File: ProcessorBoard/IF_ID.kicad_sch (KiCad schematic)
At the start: 7 parts, among them U60 74ABT32, U61 74ABT16374, U62 74ABT16374

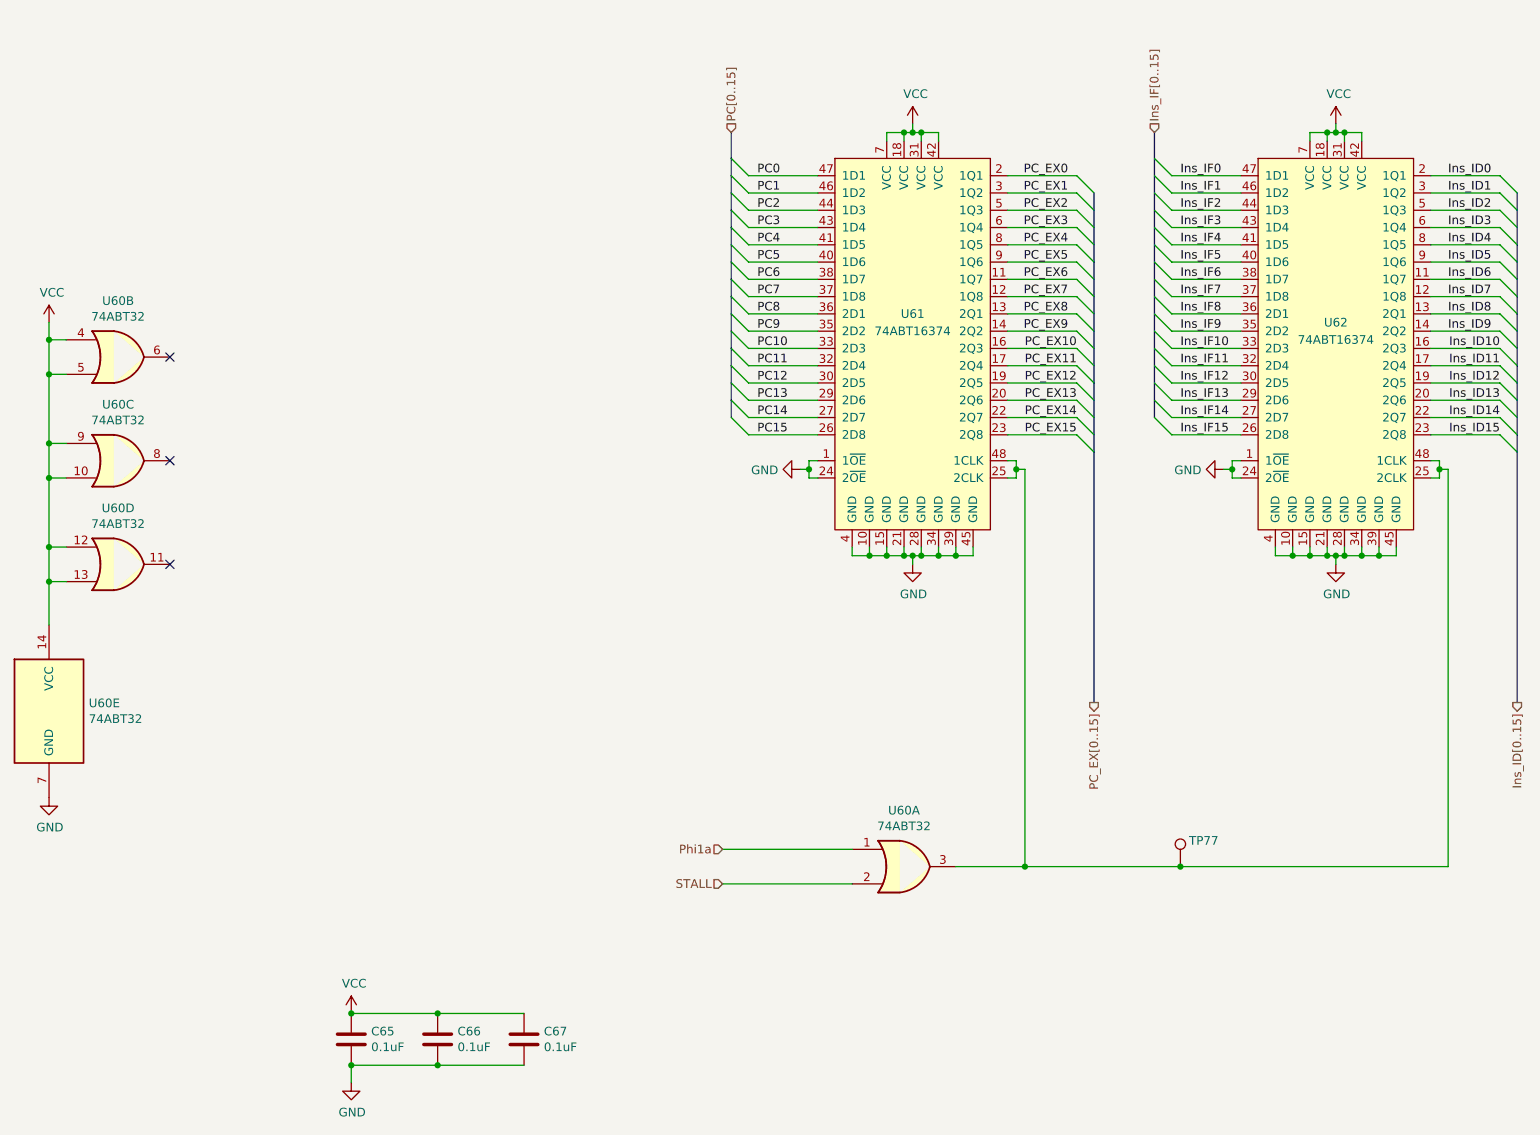
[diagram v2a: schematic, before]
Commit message: ProcessorBoard: update to include M/S bug fix in register file
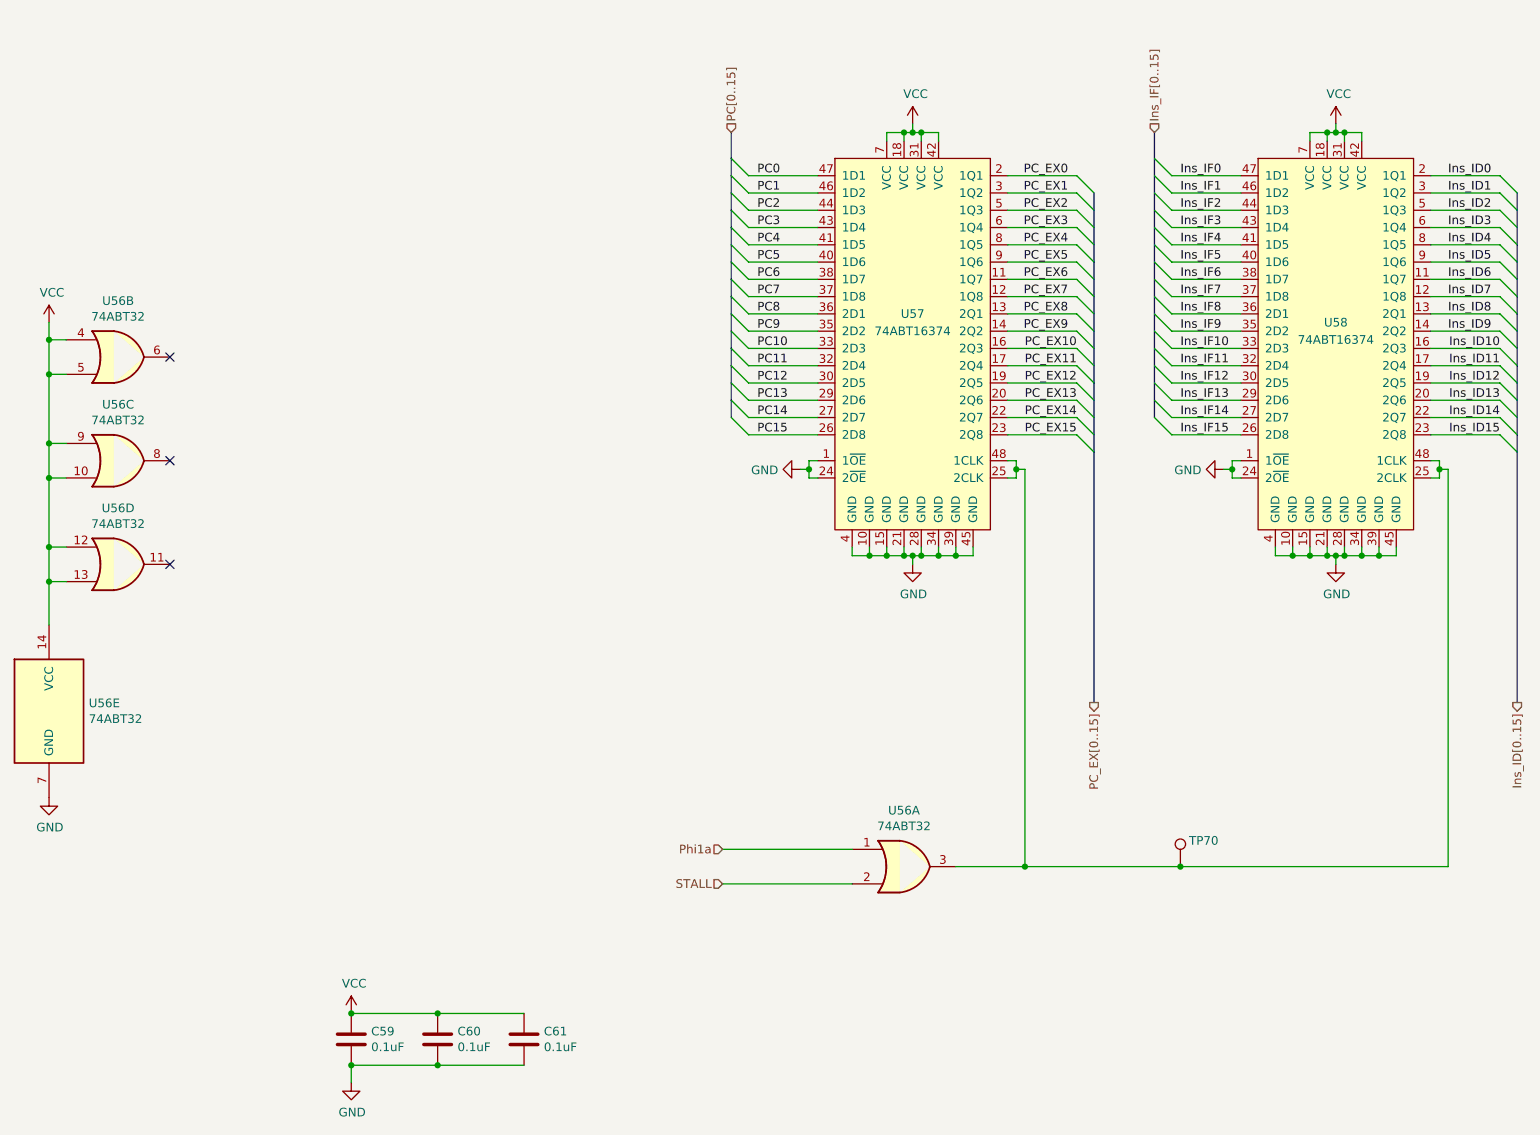
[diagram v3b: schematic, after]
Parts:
- renumbered C65 to C59, C66 to C60, C67 to C61, TP77 to TP70, U60 to U56, U61 to U57, U62 to U58

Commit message: ProcessorBoard: Replace Instruction ROM with a header for a daughter board
ROMs will be relocated to a daughter board to allow the memories and their
sockets to be swapped easily.
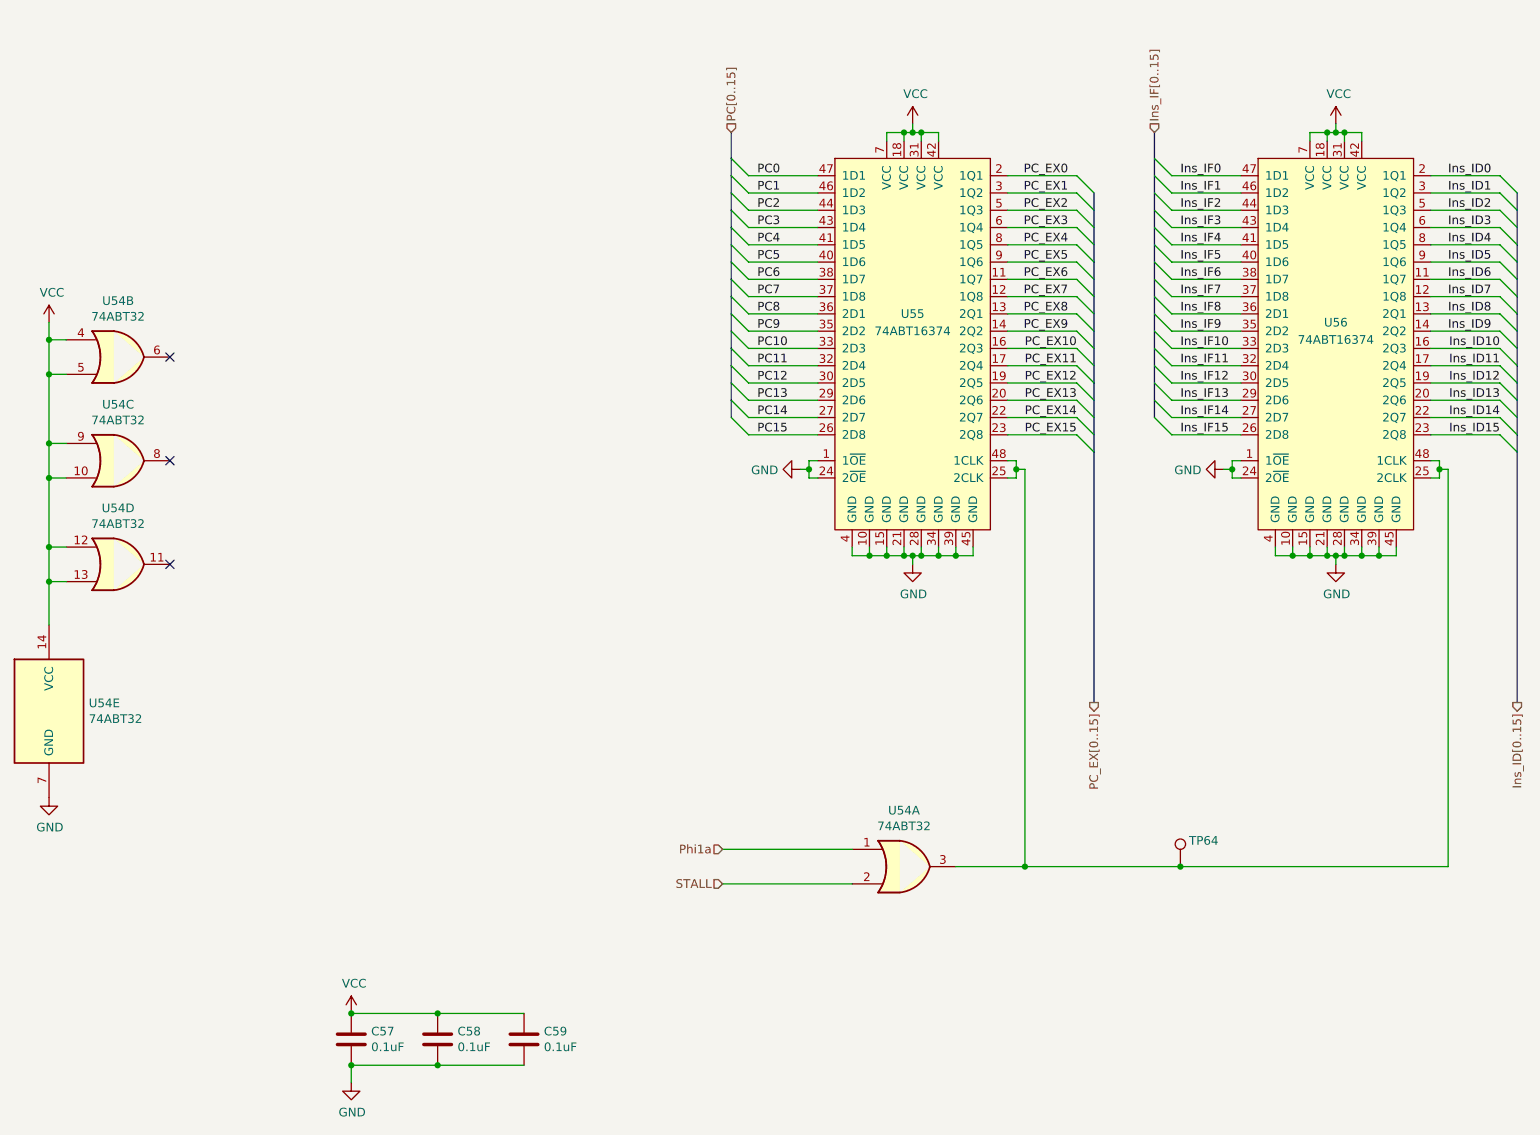
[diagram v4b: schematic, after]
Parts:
- renumbered C59 to C57, C60 to C58, C61 to C59, TP70 to TP64, U56 to U54, U57 to U55, U58 to U56

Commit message: ProcessorBoard: Copy symbols into project symbol library, make consistent
Symbols created for Turtle16 have been copied into a project-specific
symbol library. The symbols have all been updated with manufacturer,
manufacturer part number, mouser part number, and digikey part number.

Test points and mounting holes have been marked to be excluded from BOM.
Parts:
- C57, C58, C59: footprint Capacitor_SMD:C_0603_1608Metric_Pad1.08x0.95mm_HandSolder -> Capacitor_SMD:C_0603_1608Metric; Digikey# (none) -> 587-6004-1-ND; Manufacturer (none) -> Taiyo Yuden; Manufacturer# (none) -> EMK107B7104KAHT; Mouser https://www.mouser.com/ProductDetail/963-EMK107B7104KAHT -> (none); Mouser# (none) -> 963-EMK107B7104KAHT
- TP64: now left out of the parts list
- U54: symbol 74xx:74LS32 -> Turtle16:74ABT32; Digikey# (none) -> 1727-6509-1-ND; Manufacturer (none) -> Nexperia; Manufacturer# (none) -> 74ABT32PW,118; Mouser https://www.mouser.com/ProductDetail/Nexperia/74ABT32PW118?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 -> (none); Mouser# (none) -> 771-ABT32PW118
- U55, U56: symbol 74xx (kicad5):74ABT16374 -> Turtle16:74ABT16374; Digikey# (none) -> 296-3900-1-ND; Manufacturer (none) -> Texas Instruments; Manufacturer# (none) -> SN74ABT16374ADGGR; Mouser https://www.mouser.com/ProductDetail/Texas-Instruments/SN74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 -> (none); Mouser# (none) -> 595-SNABT16374ADGGR
